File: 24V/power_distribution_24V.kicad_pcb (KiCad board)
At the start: 4 copper layers, 85.2 x 56 mm, 23 parts, among them J1 39-30-1040, J2 768250002, J3 39-30-1040, J4 172065-0002, J5 39-30-1040, J6 39-30-1040, J8 768250002, U1 RASPBERRY_PCB

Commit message: corrected resistors for LEDs
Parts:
- R2, R3, R5, R6, R8: value 1.1k -> 11k
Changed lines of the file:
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@@
         (effects (font (size 1 1) (thickness 0.15)) (justify mirror))
     )
-    (fp_text value "1.1k" (at 0 -1.65) (layer "B.Fab")
+    (fp_text value "11k" (at 0 -1.65) (layer "B.Fab")
         (effects (font (size 1 1) (thickness 0.15)) (justify mirror))
     )
@@
         (effects (font (size 1 1) (thickness 0.15)) (justify mirror))
     )
-    (fp_text value "1.1k" (at 0 -1.65) (layer "B.Fab")
+    (fp_text value "11k" (at 0 -1.65) (layer "B.Fab")
         (effects (font (size 1 1) (thickness 0.15)) (justify mirror))
     )
@@
         (effects (font (size 1 1) (thickness 0.15)) (justify mirror))
     )
-    (fp_text value "1.1k" (at 0 -1.65) (layer "B.Fab")
+    (fp_text value "11k" (at 0 -1.65) (layer "B.Fab")
         (effects (font (size 1 1) (thickness 0.15)) (justify mirror))
     )
@@
         (effects (font (size 1 1) (thickness 0.15)) (justify mirror))
     )
-    (fp_text value "1.1k" (at 0 -1.65) (layer "B.Fab")
+    (fp_text value "11k" (at 0 -1.65) (layer "B.Fab")
         (effects (font (size 1 1) (thickness 0.15)) (justify mirror))
     )
@@
         (effects (font (size 1 1) (thickness 0.15)) (justify mirror))
     )
-    (fp_text value "1.1k" (at 0 -1.65) (layer "B.Fab")
-        (effects (font (size 1 1) (thickness 0.15)) (justify mirror))
-    )
+    (fp_text value "11k" (at 0 -1.65) (layer "B.Fab")
+        (effects (font (size 1 1) (thickness 0.15)) (justify mirror))
+    )

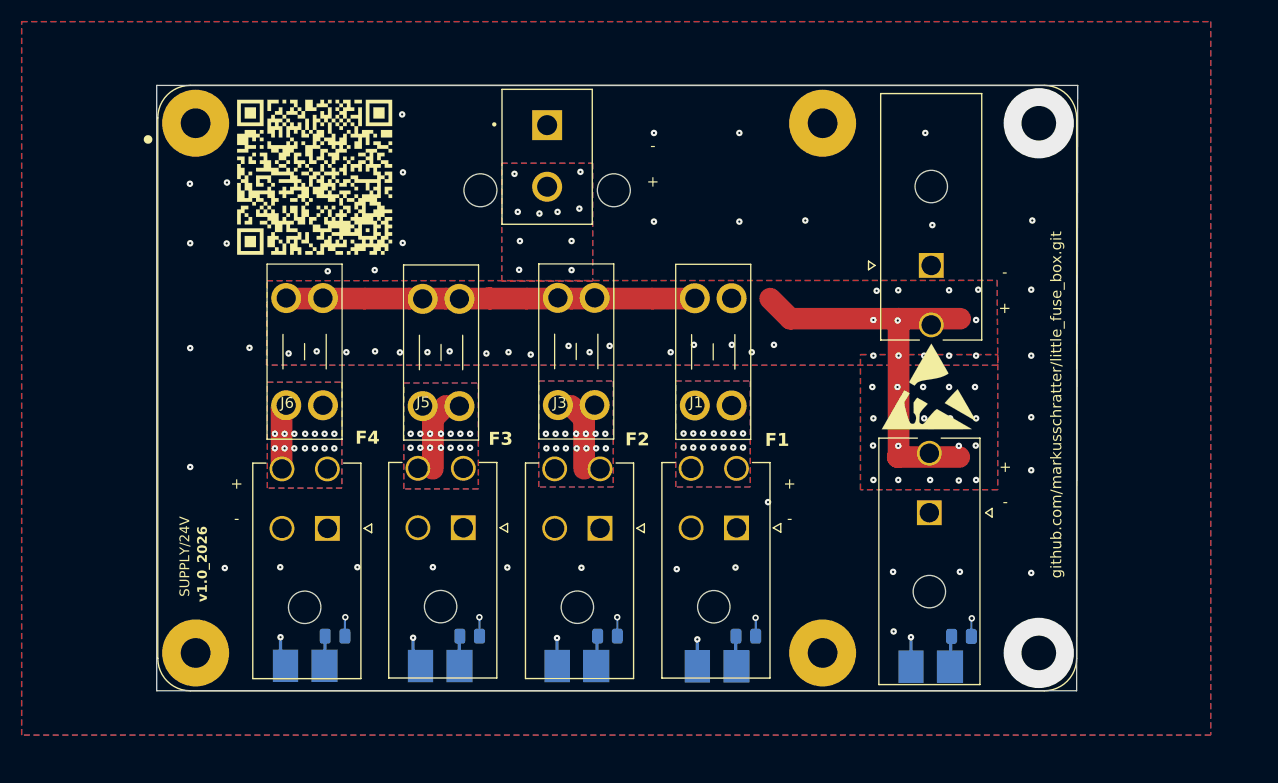
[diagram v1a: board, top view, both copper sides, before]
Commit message: changed layer priorities, increased drill hole sizes
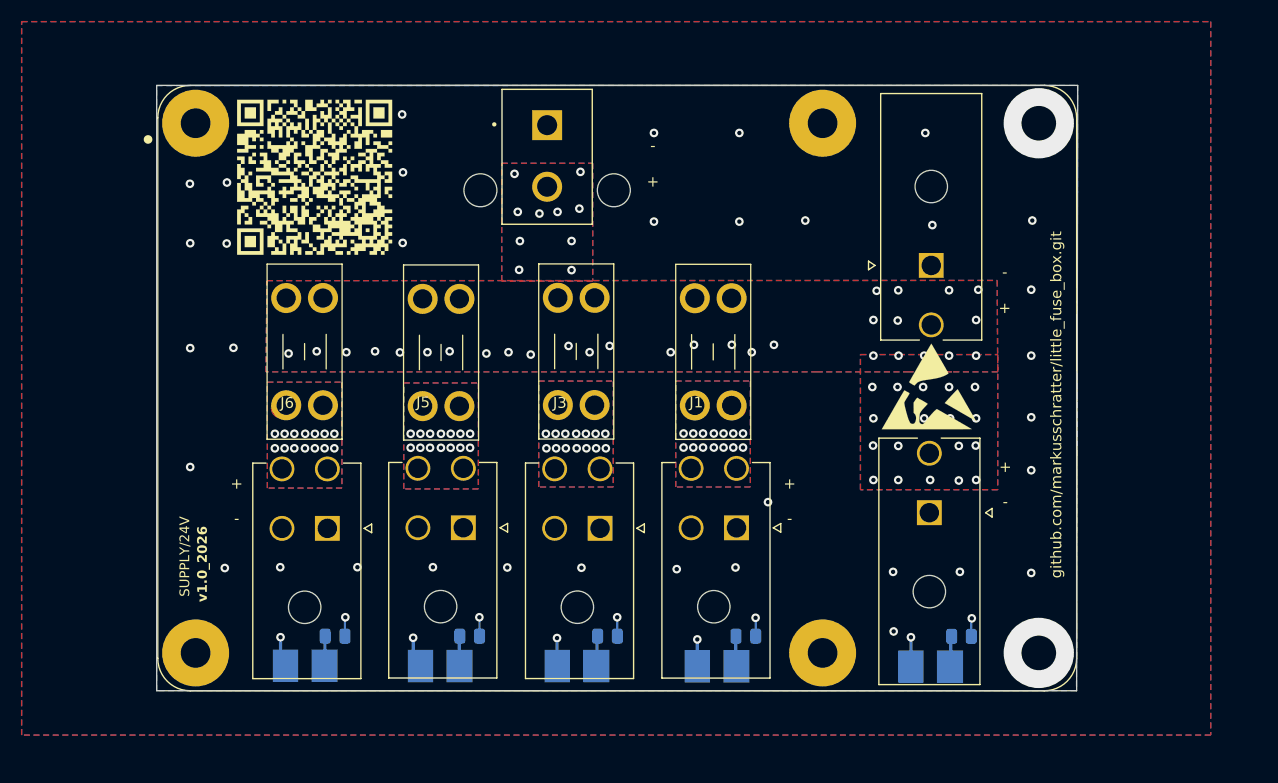
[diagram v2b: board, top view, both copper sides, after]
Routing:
- net VCC: track 78.4 -> 3.93 mm
- net Net-(D5-Pad2): track 26.7 -> 20.4 mm
- net Net-(D3-Pad2): track 26.9 -> 20.6 mm
- net Net-(D7-Pad2): track 26.6 -> 21.0 mm
- net GND: vias 42 -> 40
- added copper zone on In1.Cu, net Net-(D1-Pad2)
- added copper zone on In2.Cu, net Net-(D1-Pad2)
- added copper zone on In1.Cu, net Net-(D3-Pad2)
- added copper zone on In2.Cu, net Net-(D3-Pad2)
- added copper zone on In1.Cu, net Net-(D5-Pad2)
- added copper zone on In2.Cu, net Net-(D5-Pad2)
- added copper zone on B.Cu, net Net-(D7-Pad1)
- added copper zone on In1.Cu, net Net-(D7-Pad1)
- added copper zone on In1.Cu, net Net-(D7-Pad2)
- added copper zone on In2.Cu, net Net-(D7-Pad2)
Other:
- board text removed: "F1"
- board text removed: "F2"
- board text removed: "F3"
- board text removed: "F4"

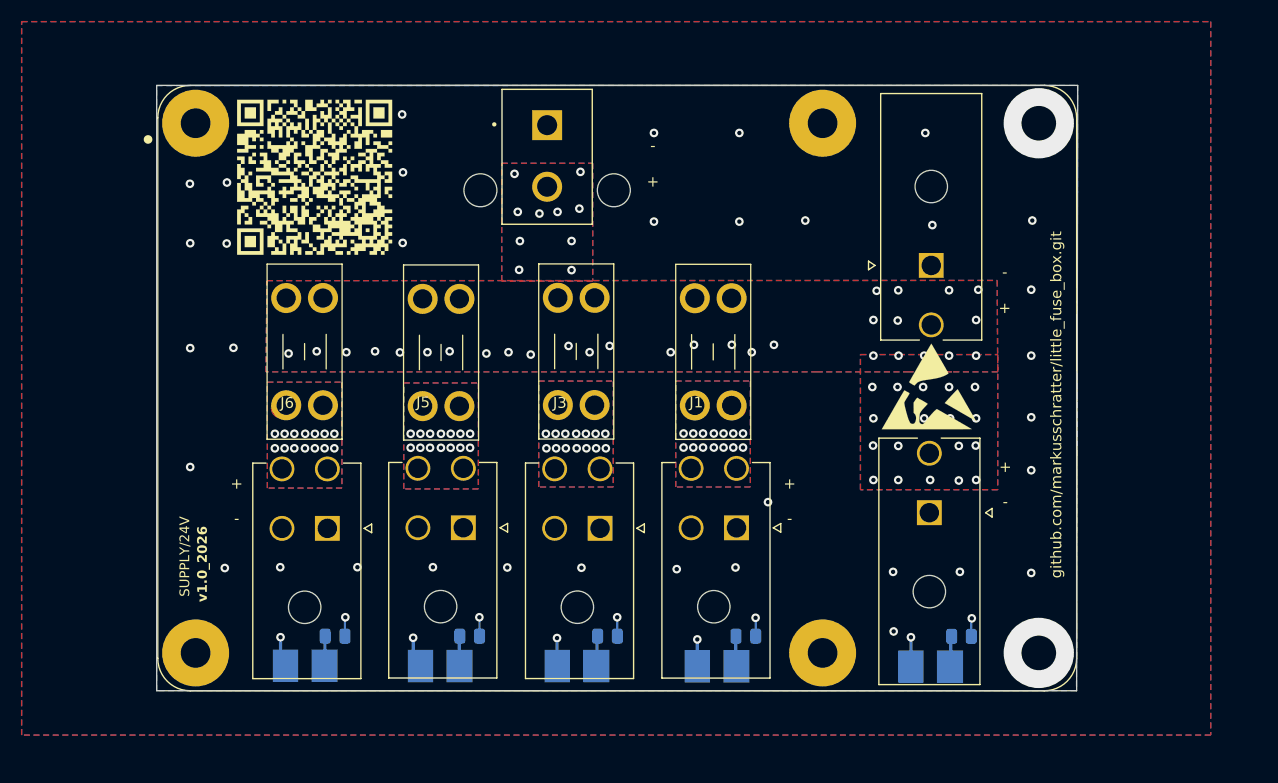
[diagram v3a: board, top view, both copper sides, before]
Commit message: added 3d model of the board and changeg layer priorities for 24V version
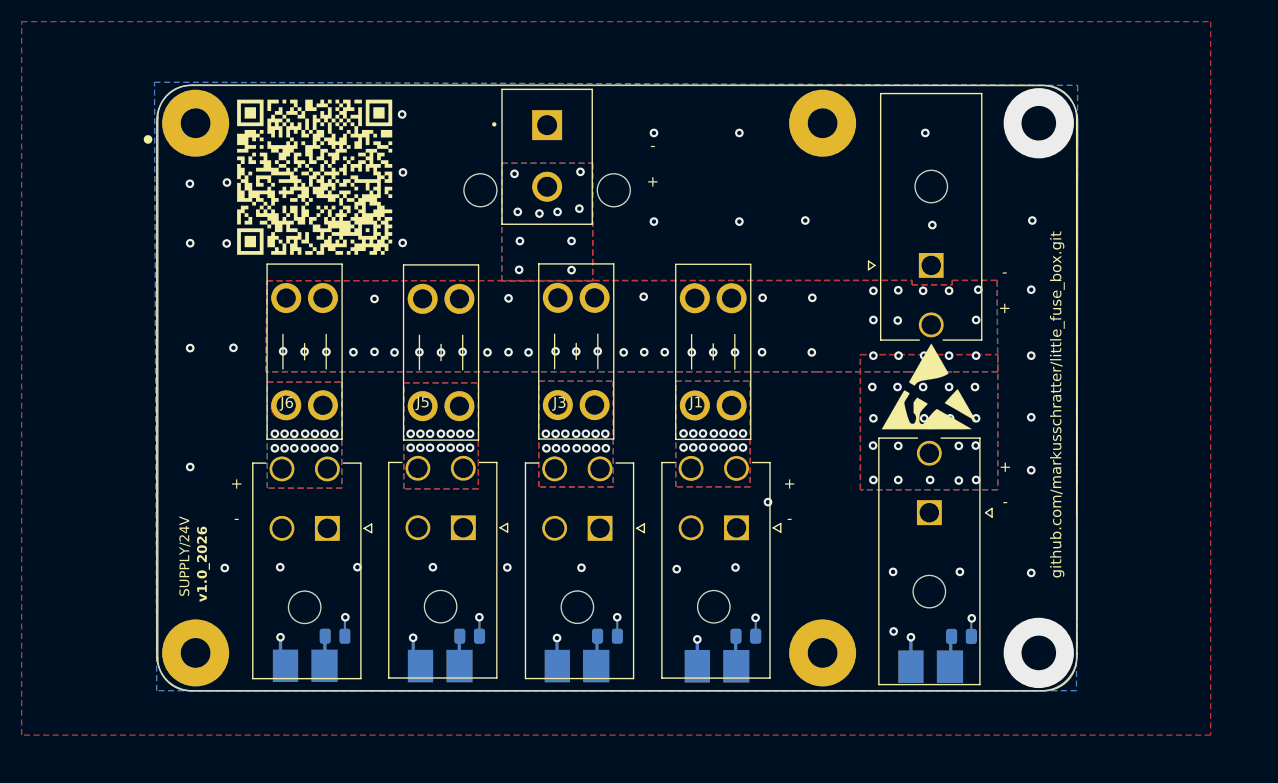
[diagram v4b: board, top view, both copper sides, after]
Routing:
- net VCC: track 3.93 -> 19.9 mm, vias 61 -> 71
- added copper zone on F.Cu, net GND
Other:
- outline, holes or cut-outs redrawn

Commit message: minor changes
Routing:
- net VCC: track 19.9 -> 3.93 mm
- removed copper zone on B.Cu, net Net-(D7-Pad1)
- removed copper zone on In1.Cu, net Net-(D7-Pad1)
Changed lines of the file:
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@@
-	)
-	(segment
-		(start 66.2 -8.4252)
-		(end 69.6722 -4.953)
-		(width 0.2)
-		(layer "In2.Cu")
-		(net 2)
-	)
-	(segment
-		(start 66.2 -19.5)
-		(end 66.2 -8.4252)
-		(width 0.2)
-		(layer "In2.Cu")
-		(net 2)
 	)
 	(segment
@@
 		(layers "F.Cu" "B.Cu" "In1.Cu" "In2.Cu")
 		(hatch full 0.508)
-		(priority 2)
+		(priority 3)
 		(connect_pads
 			(clearance 0.25)
@@
 		(layers "F.Cu" "B.Cu" "In1.Cu" "In2.Cu")
 		(hatch full 0.508)
-		(priority 2)
+		(priority 3)
 		(connect_pads
 			(clearance 0.25)
@@
 	)
 	(zone
-		(net 9)
-		(net_name "Net-(D7-Pad1)")
-		(layers "B.Cu" "In1.Cu")
+		(net 2)
+		(net_name "VCC")
+		(layers "B.Cu" "In2.Cu")
 		(hatch edge 0.508)
 		(priority 1)
@@
 			)
 		)
+	)
+	(zone
+		(net 2)
+		(net_name "VCC")
+		(layers "B.Cu" "In2.Cu")
+		(hatch edge 0.508)
+		(connect_pads yes
+			(clearance 0.6)
+		)
+		(min_thickness 0.5)
+		(filled_areas_thickness no)
+		(fill yes
+			(thermal_gap 0.25)
+			(thermal_bridge_width 0.5)
+		)
+		(polygon
+			(pts
+				(xy 101.6 6.5) (xy -8.4 6.5) (xy -8.4 -59.5) (xy 101.6 -59.5)
+			)
+		)
